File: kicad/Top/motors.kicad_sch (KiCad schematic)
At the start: 11 parts

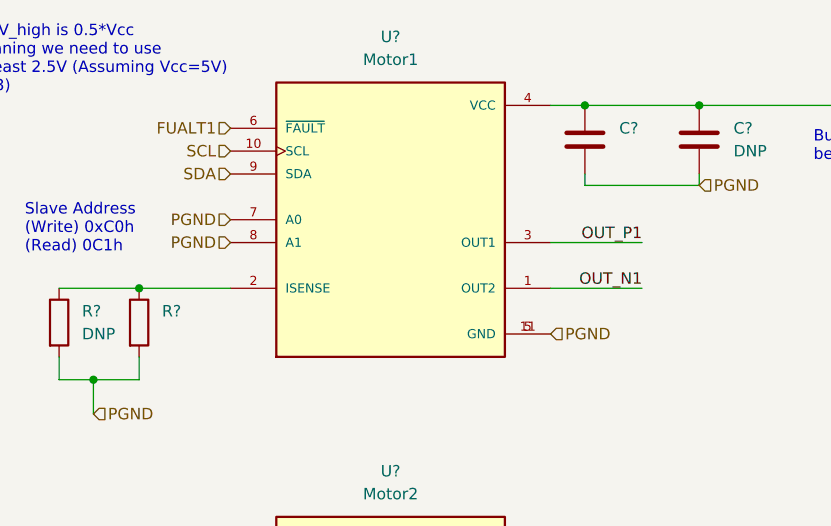
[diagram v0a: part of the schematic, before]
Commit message: Added values to passives
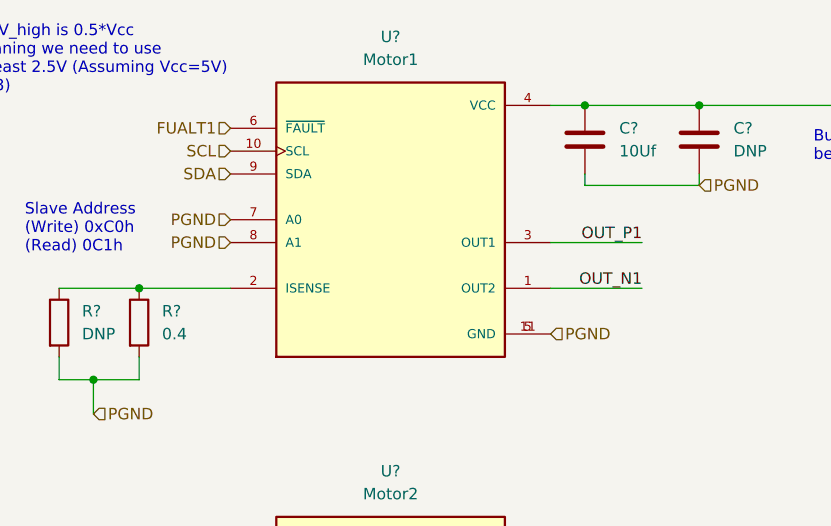
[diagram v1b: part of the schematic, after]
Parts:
- C?: value (none) -> 10Uf
- R?: value (none) -> 0.4
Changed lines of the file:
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@@
       (effects (font (size 1.27 1.27)) (justify left))
     )
-    (property "Value" "" (id 1) (at 113.03 29.2099 0)
+    (property "Value" "10Uf" (id 1) (at 113.03 29.2099 0)
       (effects (font (size 1.27 1.27)) (justify left))
     )
@@
       (effects (font (size 1.27 1.27)) (justify left))
     )
-    (property "Value" "" (id 1) (at 62.23 49.5299 0)
-      (effects (font (size 1.27 1.27)) (justify left))
-    )
+    (property "Value" "0.4" (id 1) (at 62.23 49.5299 0)
+      (effects (font (size 1.27 1.27)) (justify left))
+    )
